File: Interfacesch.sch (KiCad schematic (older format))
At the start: 15 parts

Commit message: Added schematic component for LAN9500A and started to work on the sheet for interfacing it.
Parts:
- removed J?: RJ45-TRANSFO-NEW, symbol RJ45-TRANSFO-NEW
- added J?: RJ45-TRANSFO-ACME, symbol RJ45-TRANSFO-ACME
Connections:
- wire segments 76 -> 68
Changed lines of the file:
@@
 $Descr A4 11693 8268
 encoding utf-8
-Sheet 4 4
+Sheet 4 5
 Title ""
 Date ""
@@
 	1200 3850 1200 3900
 Wire Wire Line
-	1200 3900 1300 3900
-Wire Wire Line
-	1300 3900 1400 3900
+	1200 3900 1400 3900
 Wire Wire Line
 	1300 3900 1300 3950
@@
 Connection ~ 1300 3900
 Wire Wire Line
-	1200 3350 1200 3450
-Wire Wire Line
-	1200 3450 1200 3550
-Wire Wire Line
-	1200 3450 1400 3450
-Wire Wire Line
-	1400 3450 2200 3450
+	1200 3350 1200 3550
+Wire Wire Line
+	1200 3450 2200 3450
 Wire Wire Line
 	1400 3450 1400 3550
@@
 	9300 1200 9350 1200
 Wire Wire Line
-	9350 1100 9350 1200
-Wire Wire Line
-	9350 1200 9350 1350
+	9350 1100 9350 1350
 Wire Wire Line
 	9350 1100 9400 1100
@@
 	9800 1350 9700 1350
 Wire Wire Line
-	9800 1000 9800 1100
-Wire Wire Line
-	9800 1100 9800 1350
-Wire Wire Line
-	9800 1350 9800 1450
+	9800 1000 9800 1450
 Wire Wire Line
 	9800 1100 9700 1100
@@
 	8450 2600 8400 2600
 Wire Wire Line
-	8450 2500 8450 2600
-Wire Wire Line
-	8450 2600 8450 2700
+	8450 2500 8450 2700
 Wire Wire Line
 	8450 2500 8500 2500
@@
 	1    0    0    -1
 $EndComp
-$Comp
-L RJ45-TRANSFO-NEW J?
-U 1 1 587FF427
-P 3000 1500
-F 0 "J?" H 3100 2100 50  0000 L CNN
-F 1 "RJ45-TRANSFO-NEW" H 2950 2100 50  0000 R CNN
-F 2 "" H 3000 1500 50  0000 C CNN
-F 3 "" H 3000 1500 50  0000 C CNN
-	1    3000 1500
-	1    0    0    -1
-$EndComp
 Wire Wire Line
 	1900 1800 1850 1800
 Wire Wire Line
-	1850 1800 1850 2000
-Wire Wire Line
-	1850 2000 1850 2050
+	1850 1800 1850 2050
 Wire Wire Line
 	1850 2000 1900 2000
@@
 Wire Wire Line
 	1800 1700 1900 1700
+$Comp
+L RJ45-TRANSFO-ACME J?
+U 1 1 5882703E
+P 3000 1500
+F 0 "J?" H 3100 2100 50  0000 L CNN
+F 1 "RJ45-TRANSFO-ACME" H 2950 2100 50  0000 R CNN
+F 2 "" H 3000 1500 50  0000 C CNN
+F 3 "" H 3000 1500 50  0000 C CNN
+	1    3000 1500
+	1    0    0    -1
+$EndComp
+$Sheet
+S 1950 5250 2200 1500
+U 5885429C
+F0 "USB_ETH_conv" 60
+F1 "USB_ETH_conv.sch" 60
+$EndSheet
 $EndSCHEMATC

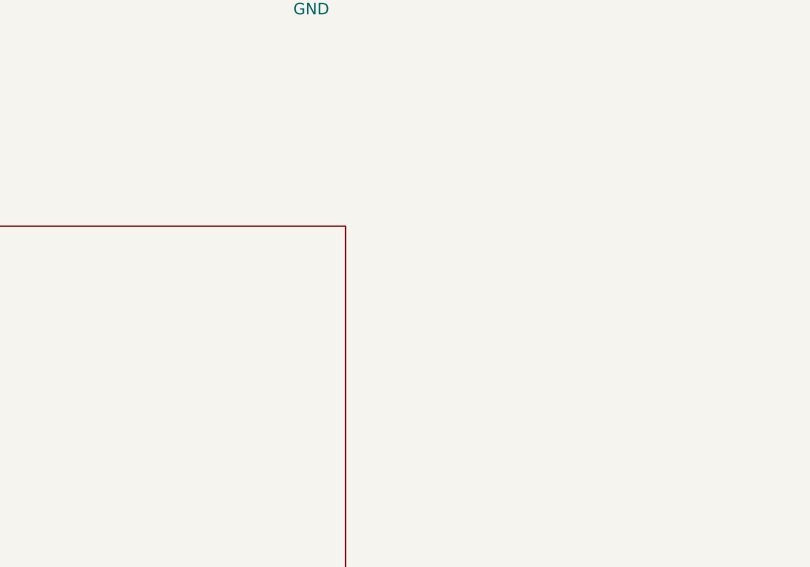
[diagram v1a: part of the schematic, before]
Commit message: Finished LAN9500A ETH to USB interface sheet.
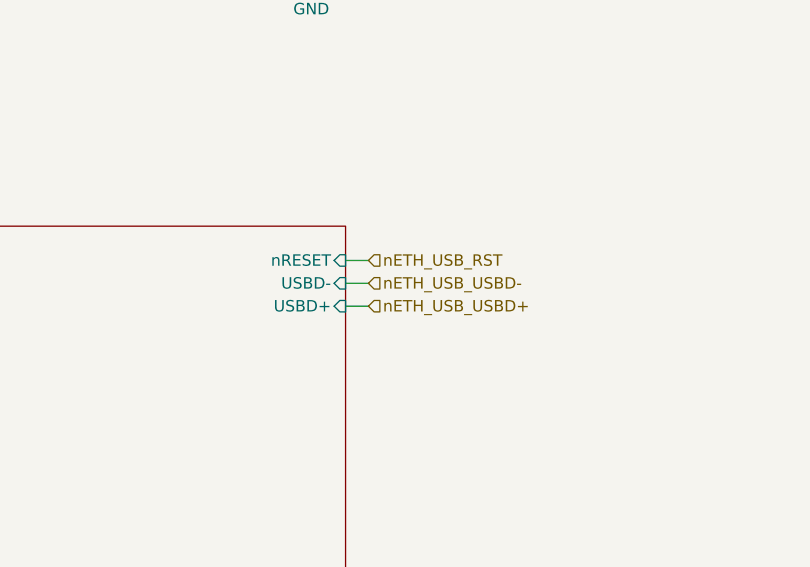
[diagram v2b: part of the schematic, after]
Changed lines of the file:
@@
 F0 "USB_ETH_conv" 60
 F1 "USB_ETH_conv.sch" 60
+F2 "nRESET" I R 4150 5400 50
+F3 "USBD-" I R 4150 5500 50
+F4 "USBD+" I R 4150 5600 50
 $EndSheet
+Text HLabel 4250 5400 2    50   Input ~ 0
+nETH_USB_RST
+Text HLabel 4250 5500 2    50   Input ~ 0
+nETH_USB_USBD-
+Text HLabel 4250 5600 2    50   Input ~ 0
+nETH_USB_USBD+
+Wire Wire Line
+	4150 5400 4250 5400
+Wire Wire Line
+	4150 5500 4250 5500
+Wire Wire Line
+	4150 5600 4250 5600
 $EndSCHEMATC
